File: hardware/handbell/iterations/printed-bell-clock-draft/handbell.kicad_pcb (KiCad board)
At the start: 2 copper layers, 44.5 x 48.3 mm, 104 parts, among them IC1 RP2040_QFN56, IC4 LSM6DSOXTR, J1 504050-0291, J2 SM02B-SRSS-TB, Q1 AO3401, Q2 C20917, Q3 DMP2045UFY4, Q4 AO3400A, Q5 CSD83325L, U1 W25Q16JVUXIQ TR / 2MB, U2 RT9080-3.3, U3 MCP73831T-2ACI/OT, U4 MAX98357A, U5 TPS61023DRLR, U6 BQ29700DSER, X6 USB Type C, Y1 12MHz/CL10pF

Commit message: Correct USB slots and lands with local VBUS and CC route repairs
Restore source-bound slot geometry and secondary-anchor process; preserve 57 remaining opens and protected returns with zero native DRC errors.

Co-authored-by: Copilot <223556219+Copilot@users.noreply.github.com>
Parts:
- X6: footprint Adafruit Feather RP2040 Prop-Maker-import-fps:USB_C_CUSB31-CFM2AX-01-X -> Handbell:USB_C_HRO_TYPE_C_31_M_12_Handbell
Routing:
- net VBUS: track 41.3 -> 34.4 mm

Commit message: Complete all 83 native part identities in one geometry-preserving batch
Apply the remaining 17 selected device and power identities; retain source geometry and publish one complete-identity schematic view.

Co-authored-by: Copilot <223556219+Copilot@users.noreply.github.com>
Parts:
- L1: value 1uH (MPN pending) -> 1uH
- Q2: value C20917 -> AO3400A

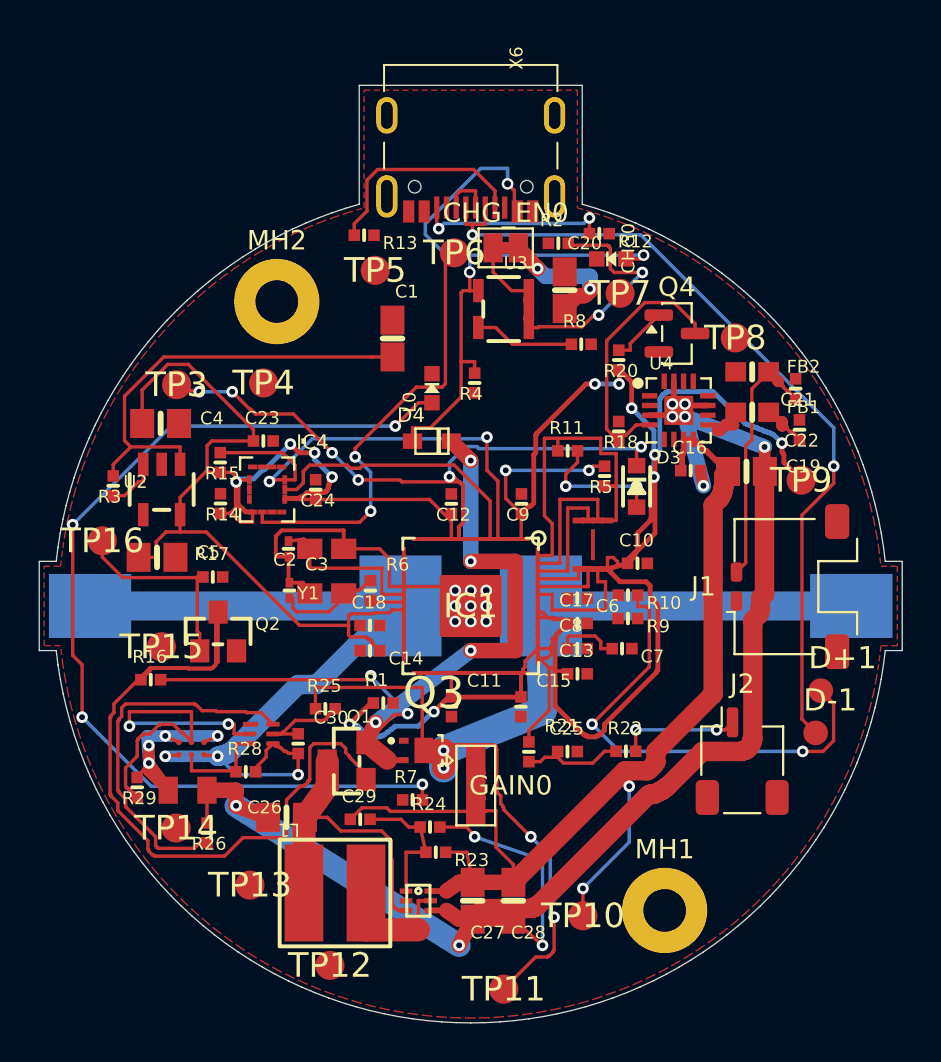
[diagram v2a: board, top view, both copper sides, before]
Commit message: Land selected power footprints and publish standalone ground checks
Preserve existing copper and quiet pickoffs across eleven land revisions. Publish the source-bound 56-open checkpoint, reusable fill plan/checker, and owner-requested pause handoff.

Co-authored-by: Copilot <223556219+Copilot@users.noreply.github.com>
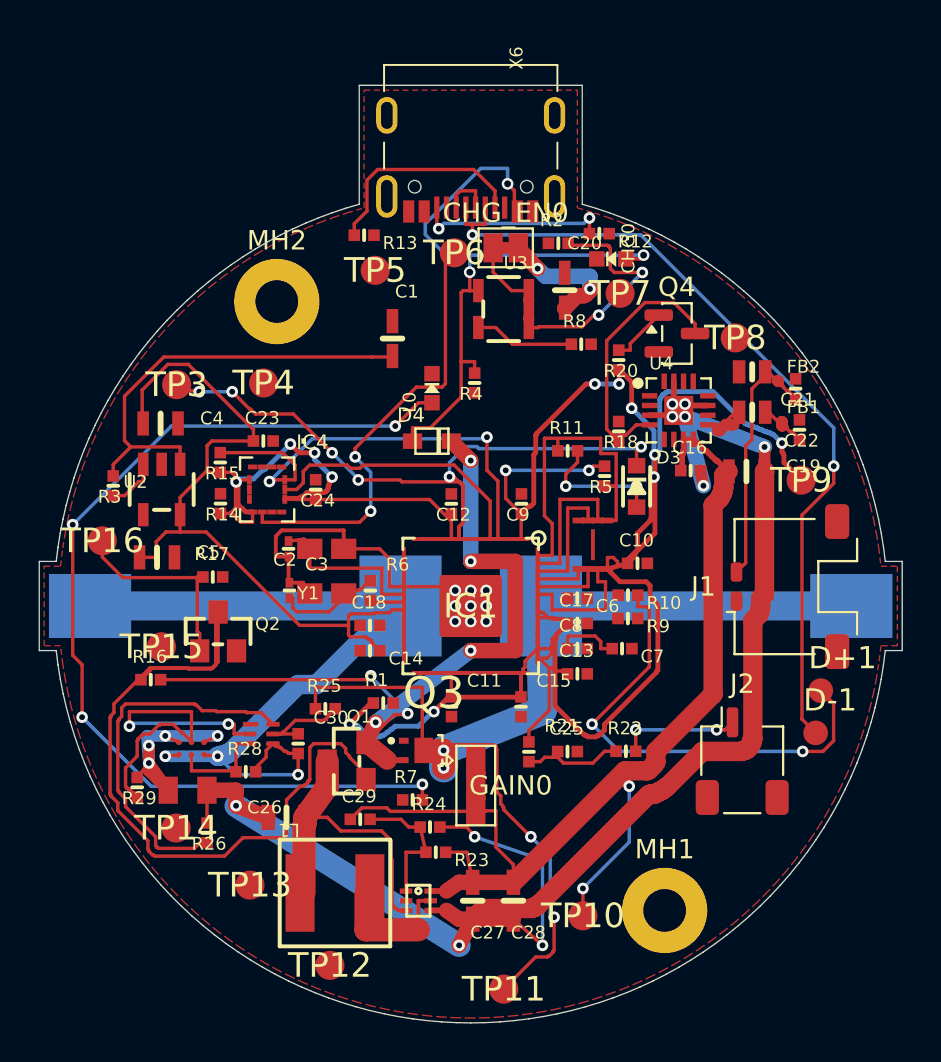
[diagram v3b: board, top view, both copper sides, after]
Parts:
- C1, C19, C20, C4, C5: footprint Adafruit Feather RP2040 Prop-Maker-import-fps:0805-NO -> Handbell:Murata_GRM21_10uF_Reflow
- C26, C27, C28: footprint Adafruit Feather RP2040 Prop-Maker-import-fps:0805-NO -> Handbell:Murata_GRM21_22uF_Reflow
- FB1, FB2: footprint Adafruit Feather RP2040 Prop-Maker-import-fps:0603-NO -> Handbell:Murata_BLM18SG121_WideCopper
- L1: footprint Adafruit TPS61023-import-fps:INDUCTOR_5X5MM_TDK_VLC5045 -> Handbell:TDK_VLS5045EX_Reflow

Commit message: Close boost and shunt lands with bounded local repairs
Apply recorded U5/R27 patterns and envelopes. Preserve trace widths and fixed poses; enlarge the R27.2 exclusion with its land. Reuse unaffected primitive evidence and bind the final filled continuity proof.

Co-authored-by: Copilot <223556219+Copilot@users.noreply.github.com>
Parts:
- R27: footprint T8:ERJ6BW_0805 -> Handbell:ERJ6BW_0805_Panasonic_Example
- U5: footprint Adafruit TPS61023-import-fps:SOT563 -> Handbell:TPS61023_DRL_TI_Example
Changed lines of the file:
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@@
 (property "Manufacturer" "Yageo" (at 0 0 0) (layer "F.Fab") (hide yes) (effects (font (size 1 1))))
 (property "CircuitReference" "https://www.ti.com/lit/ds/symlink/bq2970.pdf" (at 0 0 0) (layer "F.Fab") (hide yes) (effects (font (size 1 1)))))
-(footprint "T8:ERJ6BW_0805"   (layer "F.Cu") (attr smd) (property "Reference" "R27" (at 0 0) (layer "F.Fab") (effects (font (size .8 .8) (thickness .12)))
+(footprint "Handbell:ERJ6BW_0805_Panasonic_Example"   (layer "F.Cu") (attr smd) (property "Reference" "R27" (at 0 0) (layer "F.Fab") (effects (font (size .8 .8) (thickness .12)))
 ) (property "Value" "33m 1% 0.5W" (at 0 1.625) (layer "F.Fab") (hide yes) (effects (font (size .8 .8) (thickness .12)))
 ) (fp_rect (start -1 -0.625) (end 1 0.625) (stroke (width .05) (type solid)) (fill none) (layer "F.Fab")
 ) (fp_rect (start -1.75 -0.95) (end 1.75 0.95) (stroke (width .05) (type solid)) (fill none) (layer "F.CrtYd")
-) (pad "1" smd rect (at -1 0) (size 1 1.4) (layers "F.Cu" "F.Paste" "F.Mask")
+) (pad "1" smd rect (at -1.025 0.0) (size 1.15 1.4) (layers "F.Cu" "F.Paste" "F.Mask")
 (pintype "passive")
 (pinfunction "1_1")
 (net "/PROT_FET_RETURN"))
-(pad "2" smd rect (at 1 0) (size 1 1.4) (layers "F.Cu" "F.Paste" "F.Mask")
+(pad "2" smd rect (at 1.025 0.0) (size 1.15 1.4) (layers "F.Cu" "F.Paste" "F.Mask")
 (pintype "passive")
 (pinfunction "2_2")
@@
 (property "MPN" "MAX98357AETE+T" (at 0 0 0) (layer "F.Fab") (hide yes) (effects (font (size 1 1))))
 (property "Manufacturer" "Analog Devices / Maxim Integrated" (at 0 0 0) (layer "F.Fab") (hide yes) (effects (font (size 1 1)))))
-(footprint "Adafruit TPS61023-import-fps:SOT563"
+(footprint "Handbell:TPS61023_DRL_TI_Example"
 		(layer "F.Cu")
 		(property "Reference" "U5"
@@
 			(layer "F.SilkS")
 )
-		(pad "1" smd rect
-			(at -0.635 -0.5 0)
-			(size 0.65 0.275)
+		(pad "1" smd roundrect
+			(at -0.74 -0.5)
+			(size 0.67 0.3)
 			(layers "F.Cu" "F.Mask" "F.Paste")
-			(solder_mask_margin 0.0508)
+			(solder_mask_margin 0.05)
 			(solder_paste_margin 0)
 			(thermal_bridge_angle 0)
 (pintype "input")
 (pinfunction "FB_1")
-(net "BOOST_FB"))
-		(pad "2" smd rect
-			(at -0.635 0 0)
-			(size 0.65 0.275)
+(net "BOOST_FB")
+(roundrect_rratio 0.16666666666666669)
+)
+		(pad "2" smd roundrect
+			(at -0.74 0.0)
+			(size 0.67 0.3)
 			(layers "F.Cu" "F.Mask" "F.Paste")
-			(solder_mask_margin 0.0508)
+			(solder_mask_margin 0.05)
 			(solder_paste_margin 0)
 			(thermal_bridge_angle 0)
 (pintype "input")
 (pinfunction "EN_2")
-(net "POWER"))
-		(pad "3" smd rect
-			(at -0.635 0.5 0)
-			(size 0.65 0.275)
+(net "POWER")
+(roundrect_rratio 0.16666666666666669)
+)
+		(pad "3" smd roundrect
+			(at -0.74 0.5)
+			(size 0.67 0.3)
 			(layers "F.Cu" "F.Mask" "F.Paste")
-			(solder_mask_margin 0.0508)
+			(solder_mask_margin 0.05)
 			(solder_paste_margin 0)
 			(thermal_bridge_angle 0)
 (pintype "power_in")
 (pinfunction "VIN_3")
-(net "V+"))
-		(pad "4" smd rect
-			(at 0.635 0.5 0)
-			(size 0.65 0.275)
+(net "V+")
+(roundrect_rratio 0.16666666666666669)
+)
+		(pad "4" smd roundrect
+			(at 0.74 0.5)
+			(size 0.67 0.3)
 			(layers "F.Cu" "F.Mask" "F.Paste")
-			(solder_mask_margin 0.0508)
+			(solder_mask_margin 0.05)
 			(solder_paste_margin 0)
 			(thermal_bridge_angle 0)
 (pintype "power_in")
 (pinfunction "GND_4")
-(net "GND"))
-		(pad "5" smd rect
-			(at 0.635 0 0)
-			(size 0.65 0.275)
+(net "GND")
+(roundrect_rratio 0.16666666666666669)
+)
+		(pad "5" smd roundrect
+			(at 0.74 0.0)
+			(size 0.67 0.3)
 			(layers "F.Cu" "F.Mask" "F.Paste")
-			(solder_mask_margin 0.0508)
+			(solder_mask_margin 0.05)
 			(solder_paste_margin 0)
 			(thermal_bridge_angle 0)
 (pintype "passive")
 (pinfunction "SW_5")
-(net "BOOST_SW"))
-		(pad "6" smd rect
-			(at 0.635 -0.5 0)
-			(size 0.65 0.275)
+(net "BOOST_SW")
+(roundrect_rratio 0.16666666666666669)
+)
+		(pad "6" smd roundrect
+			(at 0.74 -0.5)
+			(size 0.67 0.3)
 			(layers "F.Cu" "F.Mask" "F.Paste")
-			(solder_mask_margin 0.0508)
+			(solder_mask_margin 0.05)
 			(solder_paste_margin 0)
 			(thermal_bridge_angle 0)
 (pintype "power_out")
 (pinfunction "VOUT_6")
-(net "VAMP"))
+(net "VAMP")
+(roundrect_rratio 0.16666666666666669)
+)
 		(embedded_fonts no)
 (at 97.300000 115.200000 0)
-(property "MPN" "TPS61023DRLR" (at 0 0) (layer "F.Fab") (hide yes) (effects (font (size 1 1) (thickness 0.15)))))
+(property "MPN" "TPS61023DRLR" (at 0 0) (layer "F.Fab") (hide yes) (effects (font (size 1 1) (thickness 0.15))))
+(attr smd)
+)
 (footprint "T8:BQ29700_DSE6"   (layer "F.Cu") (attr smd) (property "Reference" "U6" (at 0 0) (layer "F.Fab") (effects (font (size .8 .8) (thickness .12)))
 ) (property "Value" "BQ29700DSER" (at 0 1.75) (layer "F.Fab") (hide yes) (effects (font (size .8 .8) (thickness .12)))
@@
 (segment (start 97.300000 116.700000) (end 94.600000 116.700000) (width 1.2) (layer "F.Cu") (net "BOOST_SW"))
 (segment (start 94.600000 116.700000) (end 94.600000 114.800000) (width 1.2) (layer "F.Cu") (net "BOOST_SW"))
-(segment (start 97.935000 114.700000) (end 98.750000 114.700000) (width 0.3) (layer "F.Cu") (net "VAMP"))
-(segment (start 98.750000 114.700000) (end 99.400000 114.250000) (width 0.8) (layer "F.Cu") (net "VAMP"))
+(segment (start 97.935000 114.700000) (end 98.9 114.7) (width 0.3) (layer "F.Cu") (net "VAMP"))
+(segment (start 98.9 114.7) (end 99.400000 114.250000) (width 0.8) (layer "F.Cu") (net "VAMP"))
 (segment (start 99.400000 114.250000) (end 100.100000 114.250000) (width 0.8) (layer "F.Cu") (net "VAMP"))
 (segment (start 100.100000 114.250000) (end 102.200000 114.250000) (width 0.8) (layer "F.Cu") (net "VAMP"))
-(segment (start 97.935000 115.700000) (end 98.750000 115.700000) (width 0.3) (layer "F.Cu") (net "GND"))
-(segment (start 98.750000 115.700000) (end 99.400000 116.150000) (width 0.8) (layer "F.Cu") (net "GND"))
+(segment (start 97.935000 115.700000) (end 98.9 115.7) (width 0.3) (layer "F.Cu") (net "GND"))
+(segment (start 98.9 115.7) (end 99.400000 116.150000) (width 0.8) (layer "F.Cu") (net "GND"))
 (segment (start 99.400000 116.150000) (end 100.100000 116.150000) (width 0.8) (layer "F.Cu") (net "GND"))
 (segment (start 100.100000 116.150000) (end 102.200000 116.150000) (width 0.8) (layer "F.Cu") (net "GND"))
@@
 (segment (start 103.620000 100.000000) (end 119.630000 100.000000) (width 1.5) (layer "B.Cu") (net "VBAT"))
 (segment (start 96.380000 100.000000) (end 80.370000 100.000000) (width 1.5) (layer "B.Cu") (net "/CELL_NEG"))
-(segment (start 96.665000 115.700000) (end 96.250000 115.700000) (width 0.1778) (layer "F.Cu") (net "V+"))
-(segment (start 96.250000 115.700000) (end 96.150000 115.600000) (width 0.1778) (layer "F.Cu") (net "V+"))
-(segment (start 96.150000 115.600000) (end 96.100000 115.600000) (width 0.1778) (layer "F.Cu") (net "V+"))
-(segment (start 96.100000 115.600000) (end 96.050000 115.550000) (width 0.1778) (layer "F.Cu") (net "V+"))
-(segment (start 96.050000 115.550000) (end 96.050000 115.500000) (width 0.1778) (layer "F.Cu") (net "V+"))
-(segment (start 96.050000 115.500000) (end 95.950000 115.400000) (width 0.1778) (layer "F.Cu") (net "V+"))
-(segment (start 95.950000 115.400000) (end 95.950000 113.100000) (width 0.1778) (layer "F.Cu") (net "V+"))
-(segment (start 95.950000 113.100000) (end 95.900000 113.050000) (width 0.1778) (layer "F.Cu") (net "V+"))
+(segment (start 96.665000 115.700000) (end 96.15 115.7) (width 0.1778) (layer "F.Cu") (net "V+"))
+(segment (start 96.15 115.7) (end 96.05 115.6) (width 0.1778) (layer "F.Cu") (net "V+"))
+(segment (start 96.05 115.6) (end 96.0 115.6) (width 0.1778) (layer "F.Cu") (net "V+"))
+(segment (start 96.0 115.6) (end 95.95 115.55) (width 0.1778) (layer "F.Cu") (net "V+"))
+(segment (start 95.95 115.55) (end 95.95 115.5) (width 0.1778) (layer "F.Cu") (net "V+"))
+(segment (start 95.95 115.5) (end 95.85 115.4) (width 0.1778) (layer "F.Cu") (net "V+"))
+(segment (start 95.85 115.4) (end 95.85 113.1) (width 0.1778) (layer "F.Cu") (net "V+"))
+(segment (start 95.85 113.1) (end 95.900000 113.050000) (width 0.1778) (layer "F.Cu") (net "V+"))
 (segment (start 95.900000 113.050000) (end 95.900000 112.150000) (width 0.1778) (layer "F.Cu") (net "V+"))
 (segment (start 95.900000 112.150000) (end 95.850000 112.100000) (width 0.1778) (layer "F.Cu") (net "V+"))
@@
 		(polygon
 			(pts
-				(xy 85.648019 108.549966) (xy 87.150019 108.549966) (xy 87.150019 110.451966) (xy 85.648019 110.451966)
+				(xy 85.598019 108.549966) (xy 87.250019 108.549966) (xy 87.250019 110.451966) (xy 85.598019 110.451966)
 			)
 		)

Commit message: Route the left core decoupling link with a local 3V3 correction
Add three front-side VCORE segments and move one 3V3 bend 0.15 mm without narrowing it. Require the exact IC1.23/C18.2 connection in the reused ground checker; preserve earlier groups and capture the two remaining blocked approaches.

Co-authored-by: Copilot <223556219+Copilot@users.noreply.github.com>
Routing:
- net VCORE: track 3.40 -> 4.81 mm
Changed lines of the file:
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@@
 (segment (start 95.000000 100.400000) (end 93.850000 100.400000) (width 0.1778) (layer "F.Cu") (net "+3V3"))
 (segment (start 95.050000 100.350000) (end 95.000000 100.400000) (width 0.1778) (layer "F.Cu") (net "+3V3"))
-(segment (start 95.800000 100.350000) (end 95.050000 100.350000) (width 0.1778) (layer "F.Cu") (net "+3V3"))
-(segment (start 95.950000 100.200000) (end 95.800000 100.350000) (width 0.1778) (layer "F.Cu") (net "+3V3"))
+(segment (start 95.8 100.2) (end 95.050000 100.350000) (width 0.1778) (layer "F.Cu") (net "+3V3"))
+(segment (start 95.950000 100.200000) (end 95.8 100.2) (width 0.1778) (layer "F.Cu") (net "+3V3"))
 (segment (start 96.550000 100.200000) (end 95.950000 100.200000) (width 0.1778) (layer "F.Cu") (net "+3V3"))
 (segment (start 95.300000 102.300000) (end 95.312100 102.304900) (width 0.1778) (layer "F.Cu") (net "+3V3"))
@@
 (segment (start 101.9 77.4368) (end 101.9 78.23) (width 0.1778) (layer "B.Cu") (net "VBUS"))
 (segment (start 98.25 80.4426) (end 98.35 80.5426) (width 0.1778) (layer "F.Cu") (net "CC2"))
-)
+(segment (start 96.55 100.6) (end 95.9 100.6) (width 0.2) (layer "F.Cu") (net "VCORE"))
+(segment (start 95.9 100.6) (end 95.496551 101.003449) (width 0.2) (layer "F.Cu") (net "VCORE"))
+(segment (start 95.496551 101.003449) (end 95.31164 101.003449) (width 0.2) (layer "F.Cu") (net "VCORE")))

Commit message: Connect C6 core supply and shorten the QSPI detour
Preserve courtyard geometry through four small capacitor moves and a matching core bridge adjustment. No new vias or narrower existing tracks; retain QSPI, prior groups and private returns.

Co-authored-by: Copilot <223556219+Copilot@users.noreply.github.com>
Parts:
- moved C6 0.40 mm to (105.5, 100.0)
- moved C17 0.32 mm to (105.5, 101.2)
- moved C8 0.23 mm to (105.5, 102.4)
- moved C13 0.14 mm to (105.5, 103.6)
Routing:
- net QSPI_DATA[3]: track 6.82 -> 5.21 mm
- net VCORE: track 4.81 -> 6.12 mm
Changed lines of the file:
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@@
 (net "VCORE"))
 	(embedded_fonts no)
-(at 105.497898 99.599744 180)
+(at 105.497898 99.999744 180)
 (property "MPN" "GRM155R71C104KA88D" (at 0 0 0) (layer "F.Fab") (hide yes) (effects (font (size 1 1))))
 (property "Manufacturer" "Murata" (at 0 0 0) (layer "F.Fab") (hide yes) (effects (font (size 1 1)))))
@@
 (net "GND"))
 	(embedded_fonts no)
-(at 105.501069 102.200145 0)
+(at 105.501069 102.430145 0)
 (property "MPN" "GRM155R61E105KA12D" (at 0 0 0) (layer "F.Fab") (hide yes) (effects (font (size 1 1))))
 (property "Manufacturer" "Murata" (at 0 0 0) (layer "F.Fab") (hide yes) (effects (font (size 1 1)))))
@@
 (net "GND"))
 	(embedded_fonts no)
-(at 105.502546 103.500537 0)
+(at 105.502546 103.640537 0)
 (property "MPN" "GRM155R71C104KA88D" (at 0 0 0) (layer "F.Fab") (hide yes) (effects (font (size 1 1))))
 (property "Manufacturer" "Murata" (at 0 0 0) (layer "F.Fab") (hide yes) (effects (font (size 1 1)))))
@@
 (net "GND"))
 	(embedded_fonts no)
-(at 105.499429 100.897675 0)
+(at 105.499429 101.217675 0)
 (property "MPN" "GRM155R61E105KA12D" (at 0 0 0) (layer "F.Fab") (hide yes) (effects (font (size 1 1))))
 (property "Manufacturer" "Murata" (at 0 0 0) (layer "F.Fab") (hide yes) (effects (font (size 1 1)))))
@@
 (segment (start 108.175000 109.294700) (end 108.175000 112.177500) (width 0.1778) (layer "B.Cu") (net "VAMP"))
 (segment (start 105.785500 115.976700) (end 105.785500 114.567000) (width 0.1778) (layer "F.Cu") (net "VAMP"))
-(segment (start 106.704700 101.830900) (end 106.704700 102.200000) (width 0.1778) (layer "F.Cu") (net "VCORE"))
-(segment (start 106.422700 101.548900) (end 106.704700 101.830900) (width 0.1778) (layer "F.Cu") (net "VCORE"))
-(segment (start 105.053700 101.548900) (end 106.422700 101.548900) (width 0.1778) (layer "F.Cu") (net "VCORE"))
-(segment (start 104.993100 101.609500) (end 105.053700 101.548900) (width 0.1778) (layer "F.Cu") (net "VCORE"))
-(segment (start 104.993100 102.200100) (end 104.993100 101.609500) (width 0.1778) (layer "F.Cu") (net "VCORE"))
+(segment (start 106.7047 102.102) (end 106.704700 102.200000) (width 0.1778) (layer "F.Cu") (net "VCORE"))
+(segment (start 106.4227 101.82) (end 106.7047 102.102) (width 0.1778) (layer "F.Cu") (net "VCORE"))
+(segment (start 105.0537 101.82) (end 106.4227 101.82) (width 0.1778) (layer "F.Cu") (net "VCORE"))
+(segment (start 104.9931 101.8806) (end 105.0537 101.82) (width 0.1778) (layer "F.Cu") (net "VCORE"))
+(segment (start 104.9931 102.4301) (end 104.9931 101.8806) (width 0.1778) (layer "F.Cu") (net "VCORE"))
 (segment (start 107.295300 102.200000) (end 106.704700 102.200000) (width 0.1778) (layer "F.Cu") (net "VCORE"))
 (segment (start 102.600000 103.550000) (end 102.600000 104.700000) (width 0.1778) (layer "F.Cu") (net "+3V3"))
@@
 (segment (start 103.450000 99.000000) (end 106.051448 99.000000) (width 0.1778) (layer "F.Cu") (net "QSPI_SCK"))
 (segment (start 106.051448 99.000000) (end 106.051448 98.090754) (width 0.1778) (layer "F.Cu") (net "QSPI_SCK"))
-(segment (start 103.450000 99.400000) (end 104.200000 99.400000) (width 0.1778) (layer "F.Cu") (net "QSPI_DATA[3]"))
-(segment (start 104.200000 99.400000) (end 104.200000 100.205000) (width 0.1778) (layer "F.Cu") (net "QSPI_DATA[3]"))
-(segment (start 104.200000 100.205000) (end 106.950000 100.205000) (width 0.1778) (layer "F.Cu") (net "QSPI_DATA[3]"))
-(segment (start 106.950000 100.205000) (end 106.950000 98.750000) (width 0.1778) (layer "F.Cu") (net "QSPI_DATA[3]"))
+(segment (start 103.450000 99.400000) (end 106.95 99.4) (width 0.1778) (layer "F.Cu") (net "QSPI_DATA[3]"))
+(segment (start 106.95 99.4) (end 106.950000 98.750000) (width 0.1778) (layer "F.Cu") (net "QSPI_DATA[3]"))
 (segment (start 106.950000 98.750000) (end 106.551448 98.750000) (width 0.1778) (layer "F.Cu") (net "QSPI_DATA[3]"))
 (segment (start 106.551448 98.750000) (end 106.551448 98.090754) (width 0.1778) (layer "F.Cu") (net "QSPI_DATA[3]"))
@@
 (segment (start 96.55 100.6) (end 95.9 100.6) (width 0.2) (layer "F.Cu") (net "VCORE"))
 (segment (start 95.9 100.6) (end 95.496551 101.003449) (width 0.2) (layer "F.Cu") (net "VCORE"))
-(segment (start 95.496551 101.003449) (end 95.31164 101.003449) (width 0.2) (layer "F.Cu") (net "VCORE")))
+(segment (start 95.496551 101.003449) (end 95.31164 101.003449) (width 0.2) (layer "F.Cu") (net "VCORE"))
+(segment (start 103.45 99.8) (end 104.1 99.8) (width 0.2) (layer "F.Cu") (net "VCORE"))
+(segment (start 104.1 99.8) (end 104.299744 99.999744) (width 0.2) (layer "F.Cu") (net "VCORE"))
+(segment (start 104.299744 99.999744) (end 104.989898 99.999744) (width 0.2) (layer "F.Cu") (net "VCORE")))
